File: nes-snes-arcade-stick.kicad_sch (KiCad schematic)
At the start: 35 parts

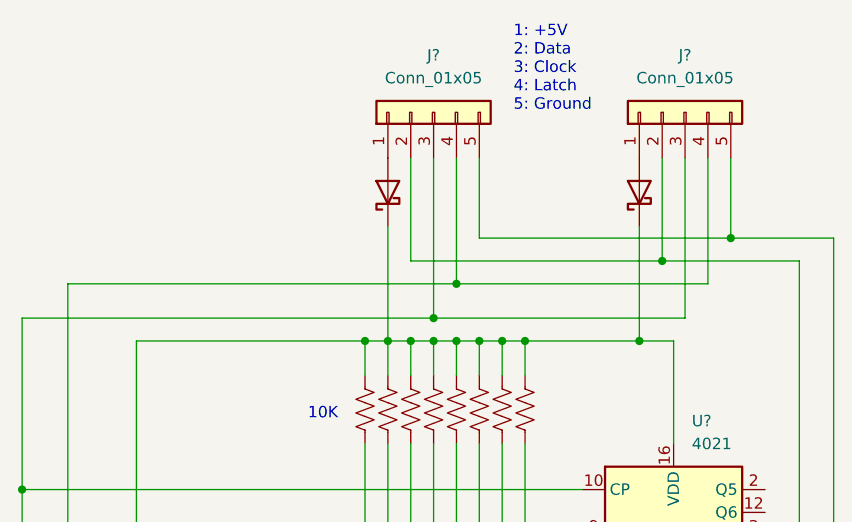
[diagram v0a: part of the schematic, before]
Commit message: update schematic
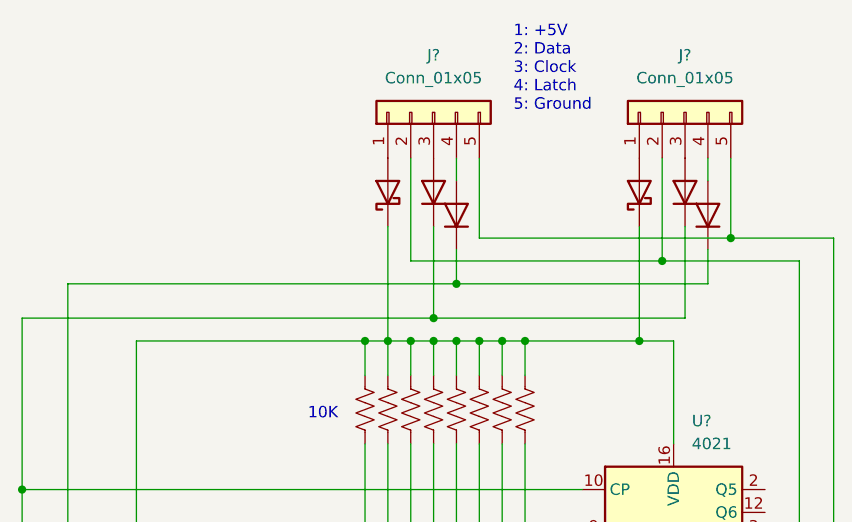
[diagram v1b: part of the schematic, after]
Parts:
- added D? (x4): 1N4148, Diode_THT:D_DO-35_SOD27_P7.62mm_Horizontal, symbol Diode:1N4148
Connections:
- net at U?.10 (CP), U?.10 (CP): now also D?.1 (K), D?.1 (K); no longer J?.3 (Pin_3), J?.3 (Pin_3)
- net at U?.9 (PL), U?.9 (PL): now also D?.1 (K), D?.1 (K); no longer J?.4 (Pin_4), J?.4 (Pin_4)
- new net: D?.2 (A), J?.4 (Pin_4) (x2)
- new net: D?.2 (A), J?.3 (Pin_3) (x2)

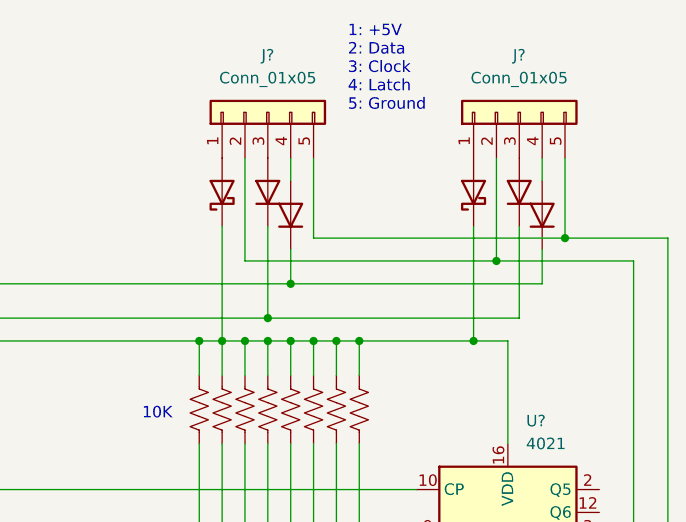
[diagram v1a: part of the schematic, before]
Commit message: removed diodes
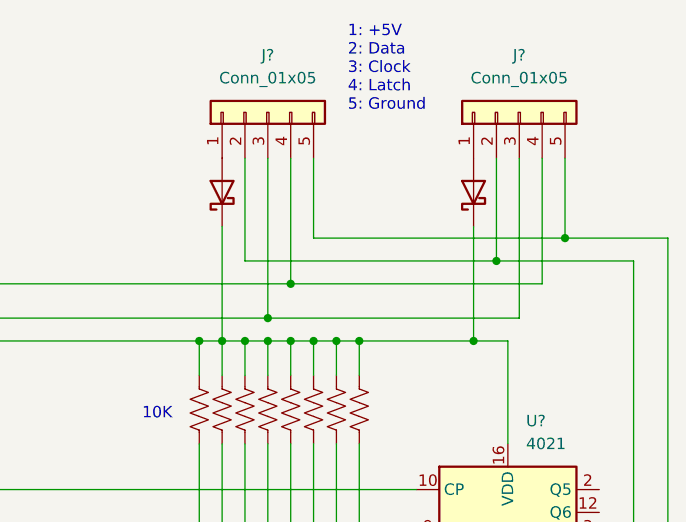
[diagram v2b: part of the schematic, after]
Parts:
- removed D? (x4): 1N4148, Diode_THT:D_DO-35_SOD27_P7.62mm_Horizontal, symbol Diode:1N4148
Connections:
- net at U?.9 (PL), U?.9 (PL): now also J?.4 (Pin_4), J?.4 (Pin_4)
- net at U?.10 (CP), U?.10 (CP): now also J?.3 (Pin_3), J?.3 (Pin_3)
